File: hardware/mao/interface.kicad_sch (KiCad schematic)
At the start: 25 parts, among them J301 LCD, J302 TOUCH TOP, J303 TOUCH REAR, SW301 SKQGADE010, U301 DRV5012AEDMRR, U302 DRV5012AEDMRR, U303 AW9364DNR

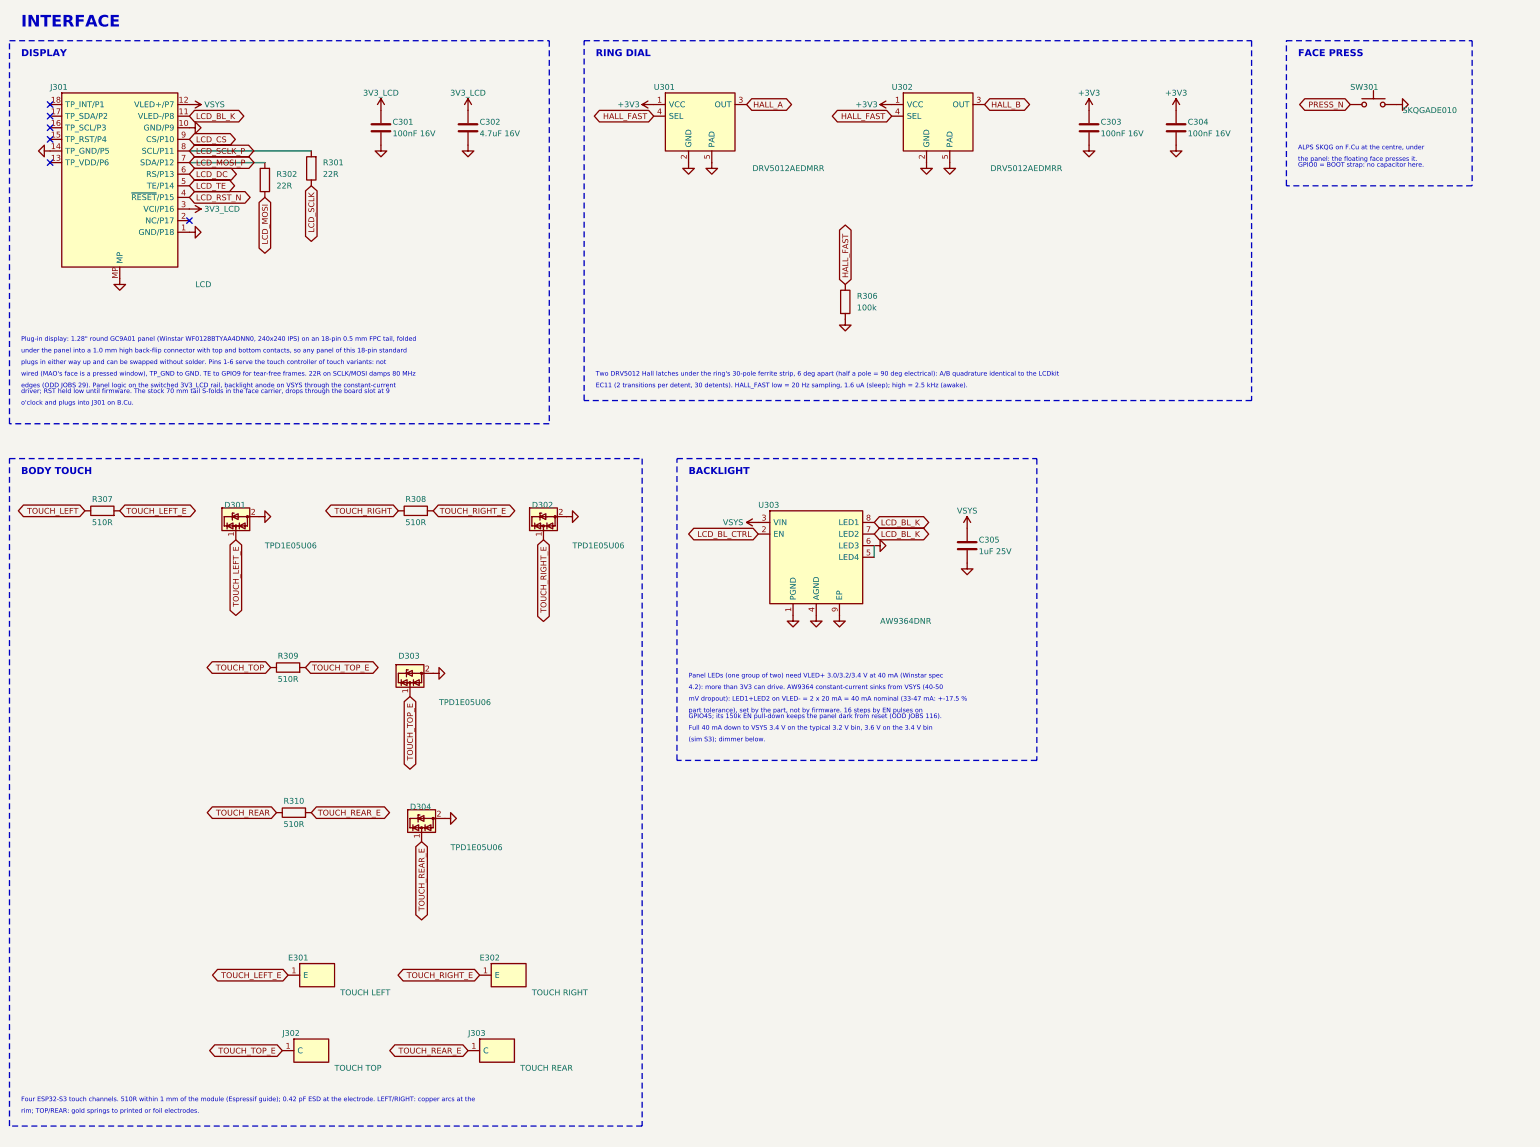
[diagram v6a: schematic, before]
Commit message: MAO A0 audit 3 fixes: VSYS feed un-necked, speaker lines over VSYS, silk leaders to their parts
Electrical audit 3 (no blocker; issue I-1):
- 11 o'clock panel tab 320 -> 328 deg: its keep-out necked the L3 VSYS band to 0.27 mm beside H1
- via-free corner where the VSYS branch turns into the backlight bar (a C205/U202 via left 0.26 mm)
- plane_check: GND and rail regions refilled at 0.5 mm minimum width must not split (necks fail
  the build); the +3V3 mesh is reported
- self-test board_id upper limit 1700 -> 1720 mV (the 3.32 V rail corner reached 1.697 V)
- comments: rail 3.10-3.32 V, AW9364 dropout, TPS22919 turn-on vs rise, panel clock, Kconfig help
- D101 drawn as a unidirectional TVS (zener glyph); module +3V3 via on C202's branch axis

ODD JOBS audit 3 (0 FAIL; recommended fixes):
- VSYS branch extended under both speaker lines (they sat over the VSYS/+3V3 zone gap); LCD_RST_N
  off L3; L3/L4 broadside 17.4 -> 13.8 mm
- EXP_RST_N's leg to TP11 designed on L3 (left to the router it detoured)
- leaders end 0.3 mm off their own part, at least 0.1 mm nearer it than any other part
- no silk text on touch-electrode copper (silk.py, mao_labels.py, check_silk_text.py): REAR and
  MIC moved
- schematic note lines on a 2.54 mm pitch (snapped 2.29 mm printed pairs that touched); tail note
- back identity on a reserved via-free spot; RSSI check with and without the LRA; drawing text
- final board: DRC 0/0/0, planes whole, no rail neck under 0.5 mm, silk 83 texts 0 findings,
  mech 0, 205 vias, 921 segments on 45 degrees; firmware 5 builds 0 warnings, 240 host checks;
  merge patch re-verified on b17187e

Co-Authored-By: Claude Opus 5.5 <noreply@anthropic.com>
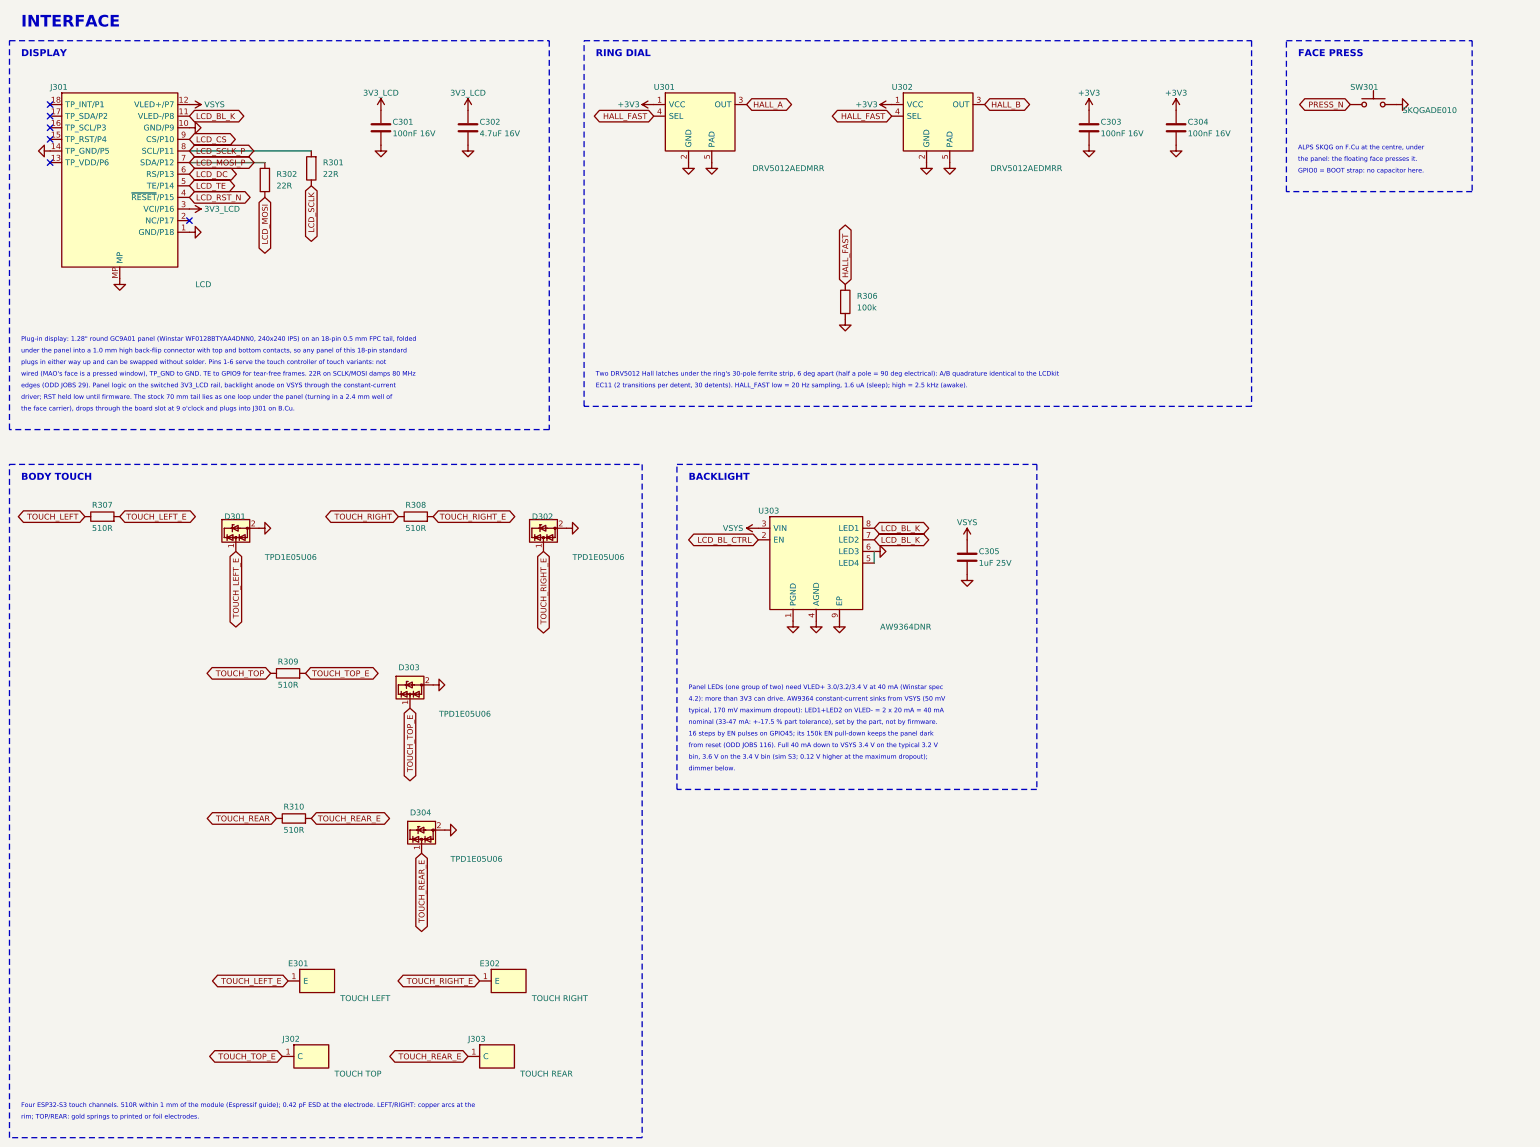
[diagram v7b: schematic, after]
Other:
- note added: "16 steps by EN pulses on GPIO45; its 150k EN pull-down keeps the panel dark"
- note added: "4.2): more than 3V3 can drive. AW9364 constant-current sinks from VSYS (50 mV"
- note added: "bin, 3.6 V on the 3.4 V bin (sim S3; 0.12 V higher at the maximum dropout);"
- note added: "dimmer below."
- note added: "driver; RST held low until firmware. The stock 70 mm tail lies as one loop under the panel (turning in a 2.4 mm well of"
- note added: "from reset (ODD JOBS 116). Full 40 mA down to VSYS 3.4 V on the typical 3.2 V"
- note added: "nominal (33-47 mA: +-17.5 % part tolerance), set by the part, not by firmware."
- note added: "the face carrier), drops through the board slot at 9 o'clock and plugs into J301 on B.Cu."
- note added: "typical, 170 mV maximum dropout): LED1+LED2 on VLED- = 2 x 20 mA = 40 mA"
- note removed: "(sim S3); dimmer below."
- note removed: "4.2): more than 3V3 can drive. AW9364 constant-current sinks from VSYS (40-50"
- note removed: "Full 40 mA down to VSYS 3.4 V on the typical 3.2 V bin, 3.6 V on the 3.4 V bin"
- note removed: "GPIO45; its 150k EN pull-down keeps the panel dark from reset (ODD JOBS 116)."
- note removed: "driver; RST held low until firmware. The stock 70 mm tail S-folds in the face carrier, drops through the board slot at 9"
- note removed: "mV dropout): LED1+LED2 on VLED- = 2 x 20 mA = 40 mA nominal (33-47 mA: +-17.5 %"
- note removed: "o'clock and plugs into J301 on B.Cu."
- note removed: "part tolerance), set by the part, not by firmware. 16 steps by EN pulses on"
- moved on the sheet: C305, D301, D302, D303, D304, E301, E302, J302, J303, R307, R308, R309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

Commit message: A1 capture: Gate C architecture on the A0 puck (schematic, ERC 0)
circuit.py now describes MAO_MAIN A1 (ERC 0 at all severities, 137 parts, 75 nets):
- ESP32-S3-MINI-1-N8 on RF_Module:ESP32-S2-MINI-1 (Gate C land audit); GPIO0 = BOOT pad only
  (10k + TP8), GPIO3/45/46 NC, 22R + DNP 10 pF on USB at the module, VBUS_SENSE 100k/150k.
- BQ25185 (ILIM/VSET 18k: 4.2 V / 500 mA; ISET 1.43k: 210 mA as A0; TS/MR to the NTC, DNP 10k,
  TSMR pad; /CE 100k pull-down; STAT1/2 10k to +3V3) replaces BQ24073.
- TPS62840 (VSET 102k = 3.2 V, SLVSEC6D table 1; 2.2 uH, CIN 4.7 uF, COUT 10 uF; MODE/STOP low,
  EN to VIN) replaces TPS63802 and its UVLO/FB dividers; LINK_REG 0R added, LINK_BAT kept.
- ICM-42670-P replaces LSM6DSOX on the same land (0x68, INT1 100k pull-up, INT2 not wired).
- DRV2605L VDD and pin 6 on +3V3; constant-current backlight sink (TLV9061 + DMG2302UK, 3.3R)
  replaces the AW9364; TPS22916C for the panel rail and the IR receiver rail.
- MAX98357A SD_MODE straight from GPIO9 (2.2k series dropped: +3V3 <= VSYS by topology).
- Removed: touch (4 zones, electrodes, springs), SPH0641, OPT3004, TCA6408A, board-ID divider.
- I2C pull-ups 4.7k; new fixture pads BL, AMP, TE, PRS, HLA, TSMR, CE, IO21, IO26.
- Battery connector stays JST SH: the Gate C JST PH side entry is 4.8 mm tall (KiCad STEP of the
  PH side-entry housing) against the 3.2 mm B-side zone over the cell; owner decision.
Parts kept from A0 keep their references; removed numbers are retired.
New footprint MAO:TI_DLC0008B_VSON-HR-8 (TI land example 4224310/A, from the Gate C generator);
A0-only custom footprints removed. Board name MAO_MAIN_A1; A0 board/outputs removed from this tree
(they stay on the A0 branch).

Co-Authored-By: Claude Opus 5.5 <noreply@anthropic.com>
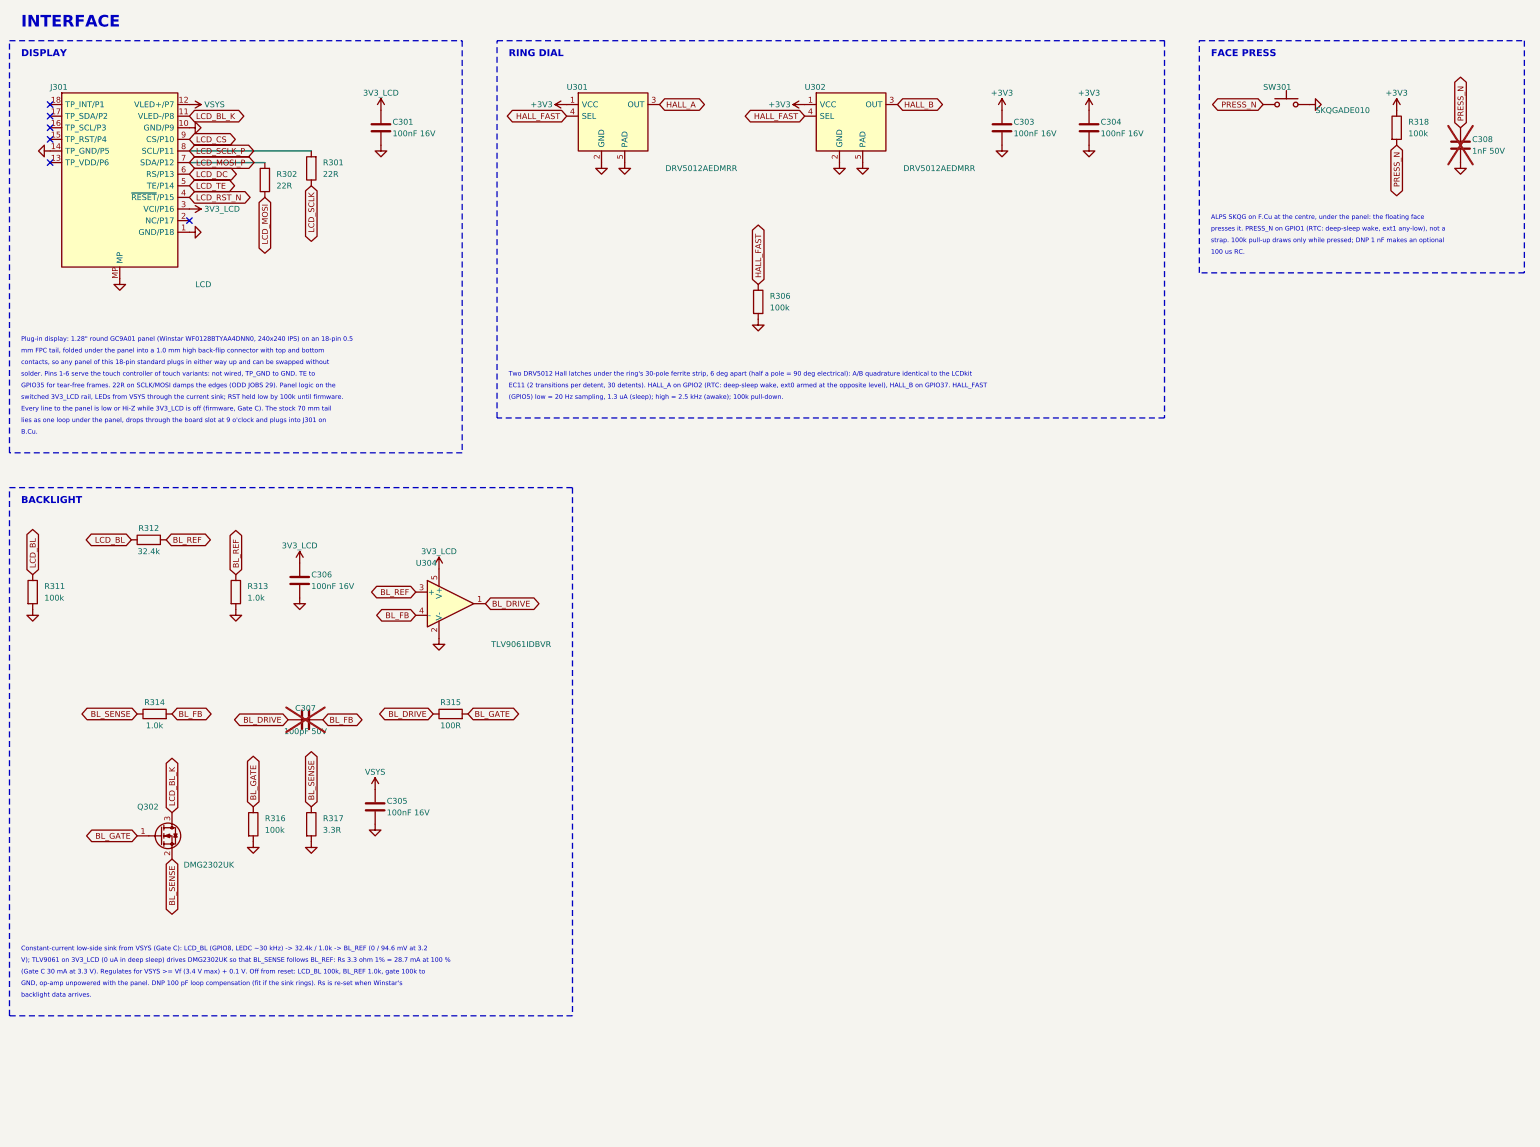
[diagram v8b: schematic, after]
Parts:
- removed C302: 4.7uF 16V, Capacitor_SMD:C_0603_1608Metric, symbol Device:C
- removed D301, D302, D303, D304: TPD1E05U06, Package_SON:Texas_DPY0002A_0.6x1mm_P0.65mm, symbol Power_Protection:TPD1E05U06DPY
- removed E301: TOUCH LEFT, MAO:TouchArc_R26.4-28.6_50deg, symbol MAO:Electrode
- removed E302: TOUCH RIGHT, MAO:TouchArc_R26.4-28.6_50deg, symbol MAO:Electrode
- removed J302: TOUCH TOP, MAO:BAT_BW0019BG_SpringContact_3.5x1.5mm, symbol MAO:Spring
- removed J303: TOUCH REAR, MAO:BAT_BW0019BG_SpringContact_3.5x1.5mm, symbol MAO:Spring
- removed R307, R308, R309, R310: 510R, Resistor_SMD:R_0402_1005Metric, symbol Device:R
- removed U303: AW9364DNR, Package_DFN_QFN:DFN-8-1EP_2x2mm_P0.5mm_EP0.6x1.2mm, symbol MAO:AW9364
- added C306: 100nF 16V, Capacitor_SMD:C_0402_1005Metric, symbol Device:C
- added C307: 100pF 50V, Capacitor_SMD:C_0402_1005Metric, symbol Device:C
- added C308: 1nF 50V, Capacitor_SMD:C_0402_1005Metric, symbol Device:C
- added Q302: DMG2302UK, Package_TO_SOT_SMD:SOT-23, symbol Transistor_FET:DMG2302U
- added R311, R316, R318: 100k, Resistor_SMD:R_0402_1005Metric, symbol Device:R
- added R312: 32.4k, Resistor_SMD:R_0402_1005Metric, symbol Device:R
- added R313, R314: 1.0k, Resistor_SMD:R_0402_1005Metric, symbol Device:R
- added R315: 100R, Resistor_SMD:R_0402_1005Metric, symbol Device:R
- added R317: 3.3R, Resistor_SMD:R_0603_1608Metric, symbol Device:R
- added U304: TLV9061IDBVR, Package_TO_SOT_SMD:SOT-23-5, symbol Amplifier_Operational:TLV9061xDBV
- C305: value 1uF 25V -> 100nF 16V; LCSC C52923 -> C1525; MPN CL05A105KA5NQNC -> CL05B104KO5NNNC
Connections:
- net +3V3: now also R318.1
- net 3V3_LCD: now also C306.1, U304.5 (V+)
- net GND: now also C306.2, C308.2, R311.2, R313.2, R316.2, R317.2, U304.2 (V-)
- net LCD_BL_K: now also Q302.3 (D)
- net PRESS_N: now also C308.1, R318.2
- new net BL_DRIVE: C307.1, R315.1, U304.1
- new net BL_FB: C307.2, R314.2, U304.4 (-)
- new net BL_GATE: Q302.1 (G), R315.2, R316.1
- new net BL_REF: R312.2, R313.1, U304.3 (+)
- new net BL_SENSE: Q302.2 (S), R314.1, R317.1
- new net LCD_BL: R311.1, R312.1
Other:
- note added: "(GPIO5) low = 20 Hz sampling, 1.3 uA (sleep); high = 2.5 kHz (awake); 100k pull-down."
- note added: "(Gate C 30 mA at 3.3 V). Regulates for VSYS >= Vf (3.4 V max) + 0.1 V. Off from reset: LCD_BL 100k, BL_REF 1.0k, gate 100k to"
- note added: "100 us RC."
- note added: "ALPS SKQG on F.Cu at the centre, under the panel: the floating face"
- note added: "B.Cu."
- note added: "Constant-current low-side sink from VSYS (Gate C): LCD_BL (GPIO8, LEDC ~30 kHz) -> 32.4k / 1.0k -> BL_REF (0 / 94.6 mV at 3.2"
- note added: "EC11 (2 transitions per detent, 30 detents). HALL_A on GPIO2 (RTC: deep-sleep wake, ext0 armed at the opposite level), HALL_B on GPIO37. HALL_FAST"
- note added: "Every line to the panel is low or Hi-Z while 3V3_LCD is off (firmware, Gate C). The stock 70 mm tail"
- note added: "GND, op-amp unpowered with the panel. DNP 100 pF loop compensation (fit if the sink rings). Rs is re-set when Winstar's"
- note added: "GPIO35 for tear-free frames. 22R on SCLK/MOSI damps the edges (ODD JOBS 29). Panel logic on the"
- note added: "Plug-in display: 1.28" round GC9A01 panel (Winstar WF0128BTYAA4DNN0, 240x240 IPS) on an 18-pin 0.5"
- note added: "V); TLV9061 on 3V3_LCD (0 uA in deep sleep) drives DMG2302UK so that BL_SENSE follows BL_REF: Rs 3.3 ohm 1% = 28.7 mA at 100 %"
- note added: "backlight data arrives."
- note added: "contacts, so any panel of this 18-pin standard plugs in either way up and can be swapped without"
- note added: "lies as one loop under the panel, drops through the board slot at 9 o'clock and plugs into J301 on"
- note added: "mm FPC tail, folded under the panel into a 1.0 mm high back-flip connector with top and bottom"
- note added: "presses it. PRESS_N on GPIO1 (RTC: deep-sleep wake, ext1 any-low), not a"
- note added: "solder. Pins 1-6 serve the touch controller of touch variants: not wired, TP_GND to GND. TE to"
- note added: "strap. 100k pull-up draws only while pressed; DNP 1 nF makes an optional"
- note added: "switched 3V3_LCD rail, LEDs from VSYS through the current sink; RST held low by 100k until firmware."
- note removed: "16 steps by EN pulses on GPIO45; its 150k EN pull-down keeps the panel dark"
- note removed: "4.2): more than 3V3 can drive. AW9364 constant-current sinks from VSYS (50 mV"
- note removed: "ALPS SKQG on F.Cu at the centre, under"
- note removed: "BODY TOUCH"
- note removed: "EC11 (2 transitions per detent, 30 detents). HALL_FAST low = 20 Hz sampling, 1.6 uA (sleep); high = 2.5 kHz (awake)."
- note removed: "Four ESP32-S3 touch channels. 510R within 1 mm of the module (Espressif guide); 0.42 pF ESD at the electrode. LEFT/RIGHT: copper arcs at the"
- note removed: "GPIO0 = BOOT strap: no capacitor here."
- note removed: "Panel LEDs (one group of two) need VLED+ 3.0/3.2/3.4 V at 40 mA (Winstar spec"
- note removed: "Plug-in display: 1.28" round GC9A01 panel (Winstar WF0128BTYAA4DNN0, 240x240 IPS) on an 18-pin 0.5 mm FPC tail, folded"
- note removed: "bin, 3.6 V on the 3.4 V bin (sim S3; 0.12 V higher at the maximum dropout);"
- note removed: "dimmer below."
- note removed: "driver; RST held low until firmware. The stock 70 mm tail lies as one loop under the panel (turning in a 2.4 mm well of"
- note removed: "edges (ODD JOBS 29). Panel logic on the switched 3V3_LCD rail, backlight anode on VSYS through the constant-current"
- note removed: "from reset (ODD JOBS 116). Full 40 mA down to VSYS 3.4 V on the typical 3.2 V"
- note removed: "nominal (33-47 mA: +-17.5 % part tolerance), set by the part, not by firmware."
- note removed: "plugs in either way up and can be swapped without solder. Pins 1-6 serve the touch controller of touch variants: not"
- note removed: "rim; TOP/REAR: gold springs to printed or foil electrodes."
- note removed: "the face carrier), drops through the board slot at 9 o'clock and plugs into J301 on B.Cu."
- note removed: "the panel: the floating face presses it."
- note removed: "typical, 170 mV maximum dropout): LED1+LED2 on VLED- = 2 x 20 mA = 40 mA"
- note removed: "under the panel into a 1.0 mm high back-flip connector with top and bottom contacts, so any panel of this 18-pin standard"
- note removed: "wired (MAO's face is a pressed window), TP_GND to GND. TE to GPIO9 for tear-free frames. 22R on SCLK/MOSI damps 80 MHz"
- title: MAO_MAIN A0 - Interface -> MAO_MAIN A1 - Interface
- moved on the sheet: C303, C304, C305, R306, SW301, U301, U302
